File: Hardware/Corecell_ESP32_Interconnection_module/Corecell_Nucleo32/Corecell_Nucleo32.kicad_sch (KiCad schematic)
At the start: 30 parts, among them IC1 PCI_EXPRESS_CARD, J1 Conn_01x19, J2 Conn_01x19, J3 Bus Standard, J4 Calculatrice_UART_groove, J5 RAK5146_UART_groove(GPS), J6 RAK5146_I2C_groove(GPS), J7 RAK5146_SPI_groove(MCU), Q1 BC548, U1 ESP32-DEVKITC-32D

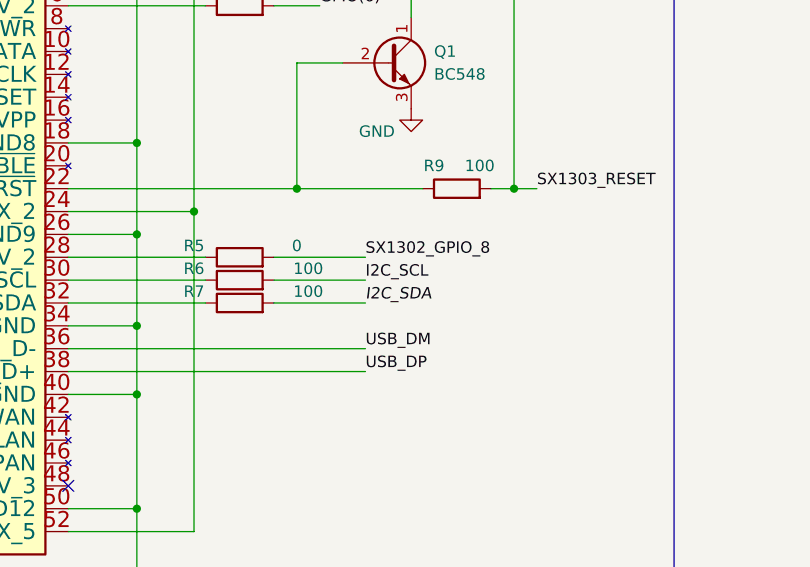
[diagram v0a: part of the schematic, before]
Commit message: New itens added to library, such as BUS from flatsat and the schematic of Nucleo.
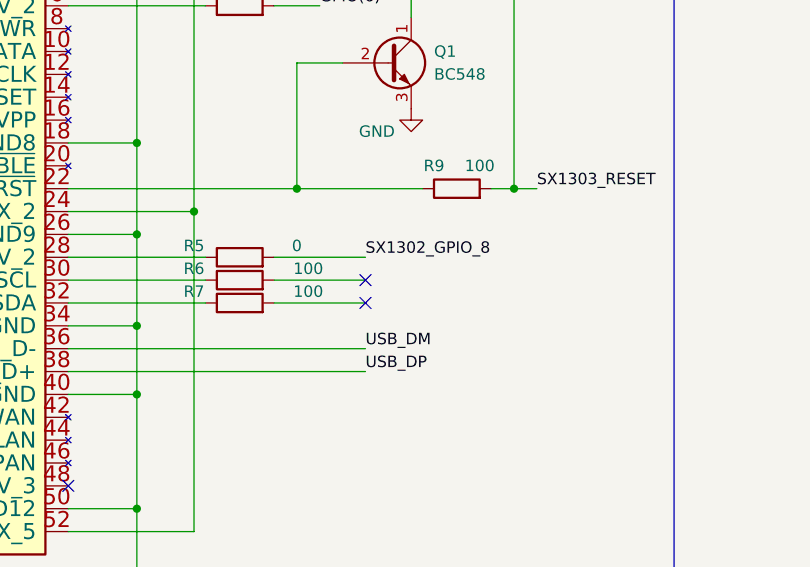
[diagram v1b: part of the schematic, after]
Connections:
- net 22: no longer R7.2
- net 25: no longer R6.2
- no-connect marks 42 -> 44
